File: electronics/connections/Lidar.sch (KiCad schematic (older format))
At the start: 0 parts

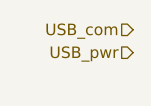
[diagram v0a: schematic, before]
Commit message: Edit button panel, edit CAD, add motor tensioners
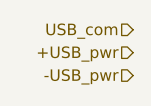
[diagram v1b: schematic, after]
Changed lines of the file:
@@
 USB_com
 Text HLabel 5950 3050 0    50   Input ~ 0
-USB_pwr
++USB_pwr
+Text HLabel 5950 3150 0    50   Input ~ 0
+-USB_pwr
 $EndSCHEMATC
